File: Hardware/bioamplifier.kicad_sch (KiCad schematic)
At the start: 28 parts, among them J1 Conn_01x40_Pin, U1 ADS1299IPAG, U7 TPS73133DBV, U8 TPS73201DCQ, X1 ECS-2520MV-xxx-xx

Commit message: Add files via upload
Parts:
- removed C26: 1 nF, Capacitor_SMD:C_0603_1608Metric_Pad1.08x0.95mm_HandSolder, symbol Device:C_Small
- removed X1: ECS-2520MV-xxx-xx, Oscillator:Oscillator_SMD_ECS_2520MV-xxx-xx-4Pin_2.5x2.0mm, symbol Oscillator:ECS-2520MV-xxx-xx
- added C40: 1 nF, Capacitor_SMD:C_0201_0603Metric, symbol Device:C_Small
- added C41: 0.1 nF, Capacitor_SMD:C_0201_0603Metric, symbol Device:C_Small
- added JP2: Jumper_2_Bridged, Jumper:SolderJumper-2_P1.3mm_Bridged2Bar_Pad1.0x1.5mm, symbol Jumper:Jumper_2_Bridged
- C1, C10, C19, C2, C20, C21, C22, C23, C24, C25, C27, C3, C4, C5, C6, C7, C8, C9: footprint Capacitor_SMD:C_0603_1608Metric_Pad1.08x0.95mm_HandSolder -> Capacitor_SMD:C_0201_0603Metric
- C29: footprint (none) -> Capacitor_SMD:C_0201_0603Metric
- JP1: footprint (none) -> Jumper:SolderJumper-2_P1.3mm_Bridged2Bar_Pad1.0x1.5mm
- R21: footprint (none) -> Resistor_SMD:R_0201_0603Metric
- U1: footprint Ads1299:PAG64_TEX -> ads1299 8channel:PAG64_TEX
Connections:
- net 3.3V_UNREG: now also C27.1
- net 5V_UNREG: now also C40.1
- net BIASINV: now also JP2.1 (A)
- net DVDD: now also C41.1
- net GNDA: now also C27.2, C29.2, U7.2 (GND), C40.2, C41.2, JP2.2 (B)
- net GNDD: now also U1.37 (CLK); no longer C27.2, C29.2, U7.2 (GND)
- net GPIO1: now also J1.31 (Pin_31); no longer J1.16 (Pin_16)
- net GPIO2: now also J1.32 (Pin_32); no longer J1.18 (Pin_18)
- net GPIO3: now also J1.33 (Pin_33); no longer J1.20 (Pin_20)
- net GPIO4: now also J1.36 (Pin_36); no longer J1.22 (Pin_22)
- removed net CLK: C27.1, U1.37 (CLK)
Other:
- note added: "8 channels at 24 bit resolution ---> minimun clock rate 110khz"
- moved on the sheet: C29, U7

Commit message: redone analog inputs, passive component footprints now match real components, added library for possible 4 element capacitor array
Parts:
- removed JP1: Jumper_2_Bridged, Jumper:SolderJumper-2_P1.3mm_Bridged2Bar_Pad1.0x1.5mm, symbol Jumper:Jumper_2_Bridged
- removed R21: 1K, Resistor_SMD:R_0201_0603Metric, symbol Device:R_Small_US
- added R1: 1K, Resistor_SMD:R_0603_1608Metric, symbol Device:R_Small_US
- C1, C19, C2, C20, C21, C4, C6, C7: footprint Capacitor_SMD:C_0201_0603Metric -> Capacitor_SMD:C_0402_1005Metric
- C10, C22, C23, C24, C25, C27, C29, C3, C40, C41, C5, C8: footprint Capacitor_SMD:C_0201_0603Metric -> Capacitor_SMD:C_0603_1608Metric
- C9: footprint Capacitor_SMD:C_0201_0603Metric -> Capacitor_SMD:C_0805_2012Metric
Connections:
- net GNDD: no longer U1.64 (RESERVED)
- net GPIO1: now also R1.2; no longer U1.42 (GPIO1)
- net SCLK: now also U1.40 (SCLK)
- net SRB2: now also U1.18 (SRB2)
- net at D1.2 (A): now also U1.42 (GPIO1); no longer U1.40 (SCLK)
- net at D1.1 (K): now also R1.1

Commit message: redone analog inputs, decoupling caps
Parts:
- C22, C23, C24: footprint Capacitor_SMD:C_0603_1608Metric -> Capacitor_SMD:C_0402_1005Metric
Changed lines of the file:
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@@
 			)
 		)
-		(property "Footprint" "Capacitor_SMD:C_0603_1608Metric"
+		(property "Footprint" "Capacitor_SMD:C_0402_1005Metric"
 			(at 194.31 88.9 0)
 			(effects
@@
 			)
 		)
-		(property "Footprint" "Capacitor_SMD:C_0603_1608Metric"
+		(property "Footprint" "Capacitor_SMD:C_0402_1005Metric"
 			(at 231.14 76.2 0)
 			(effects
@@
 			)
 		)
-		(property "Footprint" "Capacitor_SMD:C_0603_1608Metric"
+		(property "Footprint" "Capacitor_SMD:C_0402_1005Metric"
 			(at 205.486 80.01 0)
 			(effects

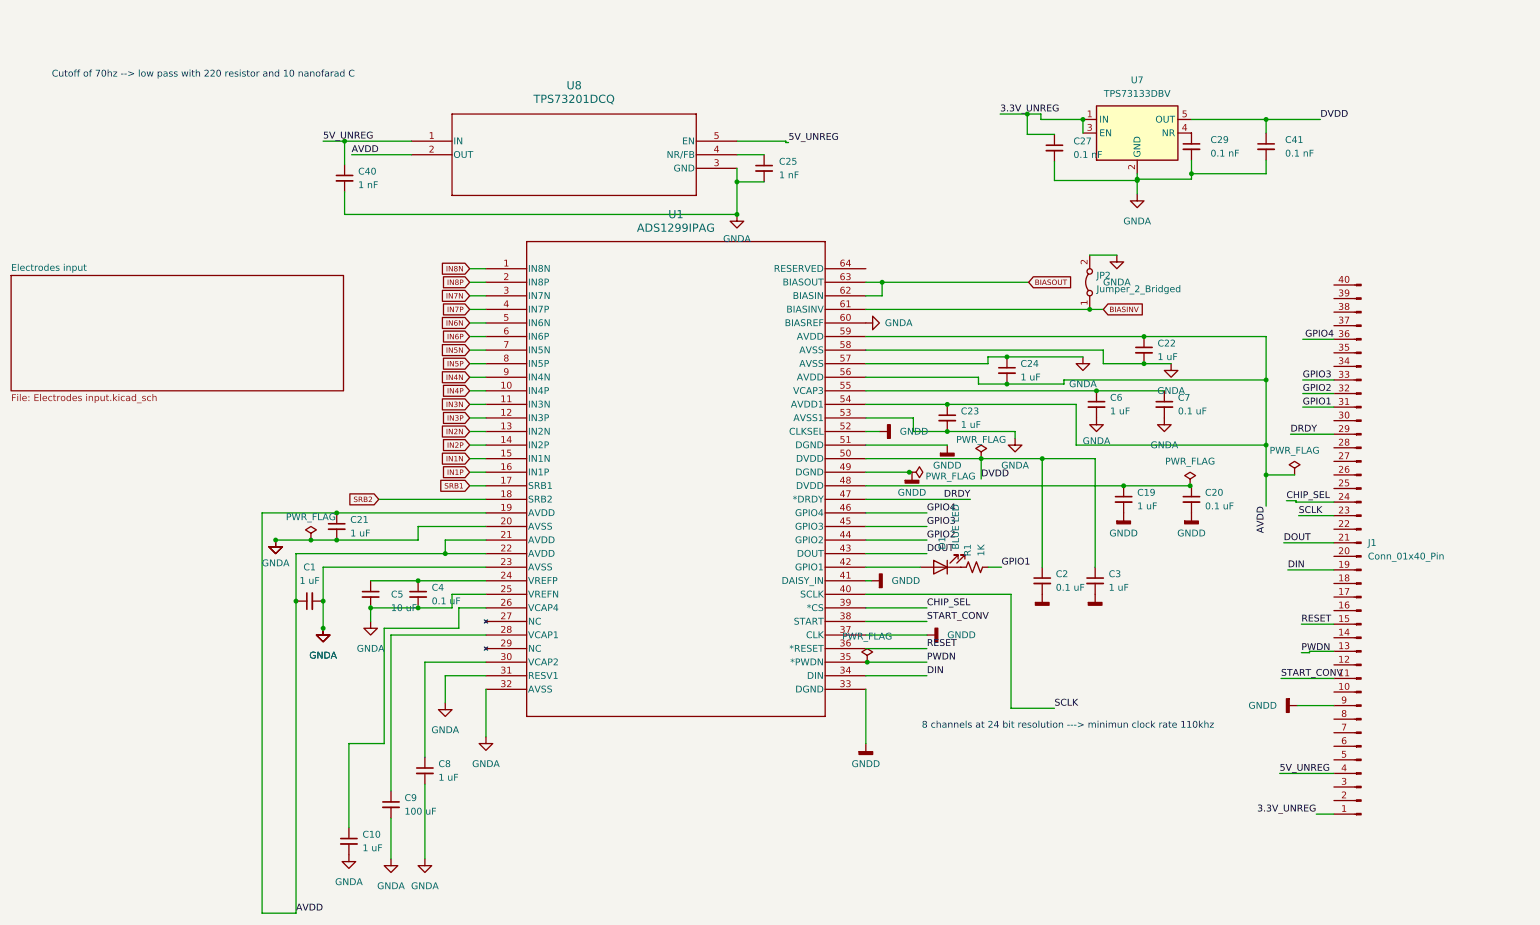
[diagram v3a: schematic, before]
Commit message: added schematics components for a bipolar power supply
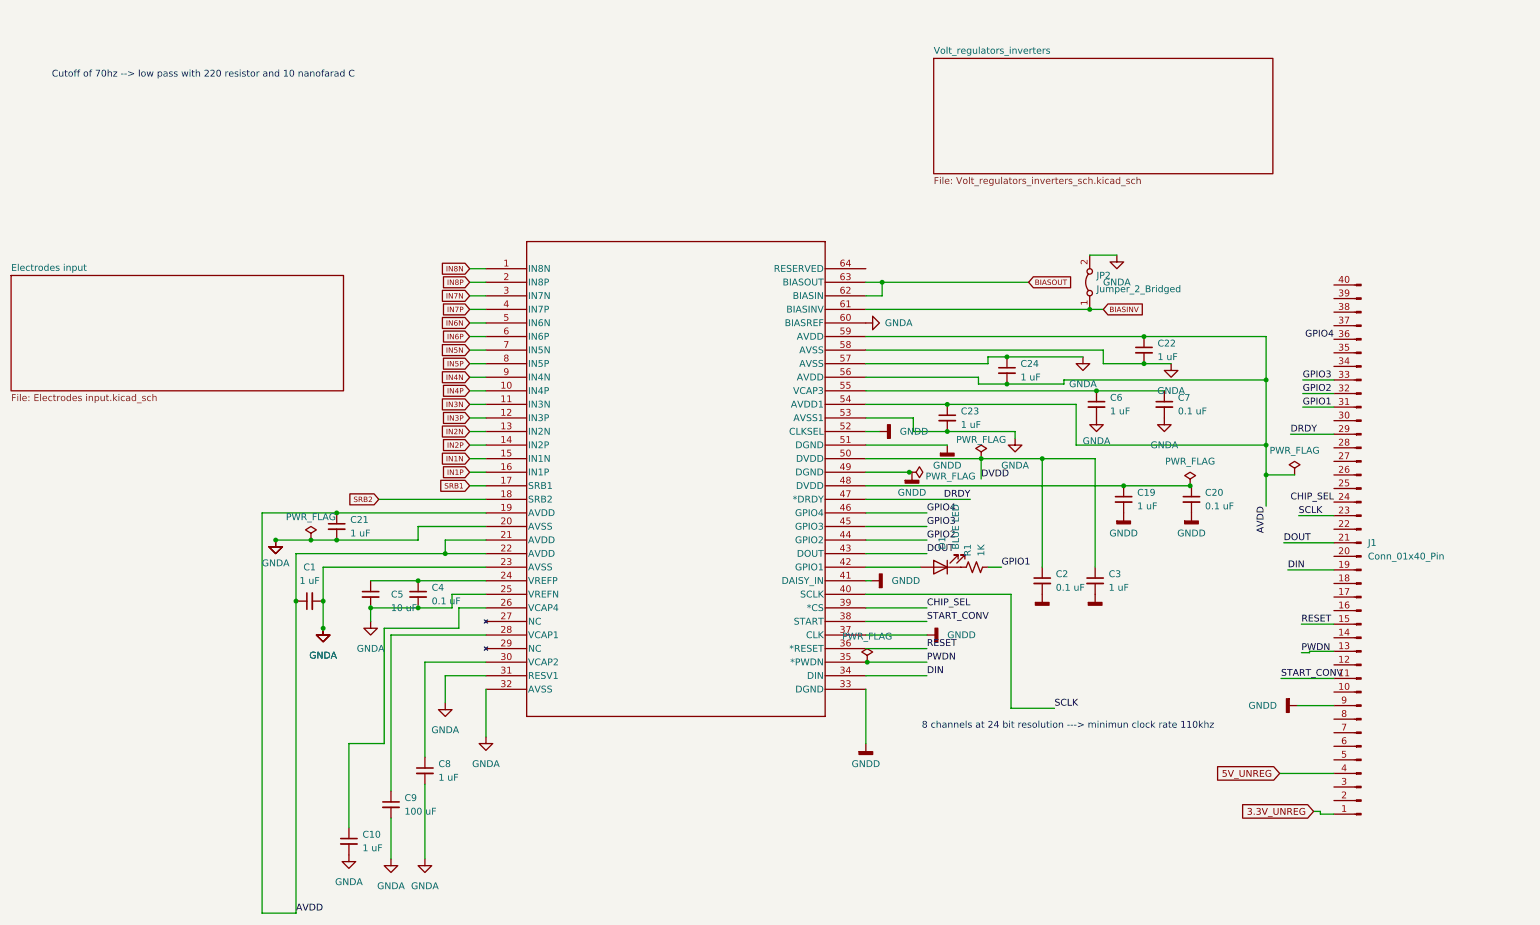
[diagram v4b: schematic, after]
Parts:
- removed C25, C40: 1 nF, Capacitor_SMD:C_0603_1608Metric, symbol Device:C_Small
- removed C27, C29, C41: 0.1 nF, Capacitor_SMD:C_0603_1608Metric, symbol Device:C_Small
- removed U7: TPS73133DBV, Package_TO_SOT_SMD:SOT-23-5, symbol Regulator_Linear:TPS73133DBV
- removed U8: TPS73201DCQ, tps732:DCQ6_TEX, symbol tps732:TPS73201DCQ
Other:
- added sheet Volt_regulators_inverters (Volt_regulators_inverters_sch.kicad_sch)

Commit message: first commit
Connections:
- net GNDA: now also C8.1; no longer C8.2
- net at U1.30 (VCAP2): now also C8.2; no longer C8.1
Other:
- moved on the sheet: C10, C21

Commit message: schematics redone, TODO: Pcb component placement
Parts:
- removed J1: Conn_01x40_Pin, Connector_PinHeader_2.54mm:PinHeader_2x20_P2.54mm_Vertical, symbol Connector:Conn_01x40_Pin
- added J1, J3: Conn_01x08_Socket, Connector_PinHeader_2.54mm:PinHeader_1x08_P2.54mm_Vertical, symbol Connector:Conn_01x08_Socket
- added R10, R11, R12, R13, R14, R15, R3, R4, R5, R6, R7, R8, R9: 50, Resistor_SMD:R_0402_1005Metric, symbol Device:R_Small_US
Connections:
- net 3.3V_UNREG: now also J3.7 (Pin_7)
- net 5V_UNREG: now also J3.8 (Pin_8)
- net CHIP_SEL: now also R6.1
- net DIN: now also R7.1
- net DOUT: now also R8.1
- net DRDY: now also R5.1
- net GNDA: now also C8.2; no longer C8.1
- net GNDD: now also J1.1 (Pin_1)
- net GPIO1: now also R12.1
- net GPIO2: now also R11.1
- net GPIO3: now also R10.1
- net GPIO4: now also R9.1
- net PWDN: now also R14.1
- net RESET: now also R13.1
- net SCLK: now also R3.1
- net START_CONV: now also R15.1, R4.1
- net at U1.30 (VCAP2): now also C8.1; no longer C8.2
- new net: J3.1 (Pin_1), R3.2
- new net: J3.5 (Pin_5), R7.2
- new net: J1.3 (Pin_3), R10.2
- new net: J1.4 (Pin_4), R11.2
- new net: J1.5 (Pin_5), R12.2
- new net: J1.2 (Pin_2), R9.2
- new net: J1.6 (Pin_6), R13.2
- new net: J1.8 (Pin_8), R15.2
- new net: J3.2 (Pin_2), R4.2
- new net: J1.7 (Pin_7), R14.2
- new net: J3.6 (Pin_6), R8.2
- new net: J3.4 (Pin_4), R6.2
- new net: J3.3 (Pin_3), R5.2
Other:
- moved on the sheet: C10, C19, C2, C24, C3, C4, C5, C7, C8, C9, JP2

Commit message: changes to pcb and schematics
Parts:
- removed J1: Conn_01x08_Socket, Connector_PinHeader_2.54mm:PinHeader_1x08_P2.54mm_Vertical, symbol Connector:Conn_01x08_Socket
- removed R15: 50, Resistor_SMD:R_0402_1005Metric, symbol Device:R_Small_US
- added J1: Conn_01x07_Socket, Connector_PinHeader_2.54mm:PinHeader_1x07_P2.54mm_Vertical, symbol Connector:Conn_01x07_Socket
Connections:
- net 3.3V_UNREG: now also J3.8 (Pin_8); no longer J3.7 (Pin_7)
- net 5V_UNREG: now also J3.7 (Pin_7); no longer J3.8 (Pin_8)
- net CHIP_SEL: now also R10.1; no longer R6.1
- net DIN: now also R14.1; no longer R7.1
- net DOUT: now also R7.1; no longer R8.1
- net DRDY: now also R3.1; no longer R5.1
- net GNDD: now also J1.1 (Pin_1)
- net GPIO1: now also R8.1; no longer R12.1
- net GPIO2: now also R6.1; no longer R11.1
- net GPIO3: now also R5.1; no longer R10.1
- net GPIO4: now also R4.1; no longer R9.1
- net PWDN: now also R13.1; no longer R14.1
- net RESET: now also R12.1; no longer R13.1
- net SCLK: now also R9.1; no longer R3.1
- net START_CONV: now also R11.1; no longer R4.1
- net at R10.2: now also J1.3 (Pin_3)
- net at R11.2: now also J1.4 (Pin_4)
- net at R12.2: now also J1.5 (Pin_5)
- net at R9.2: now also J1.2 (Pin_2)
- net at R13.2: now also J1.6 (Pin_6)
- net at R14.2: now also J1.7 (Pin_7)

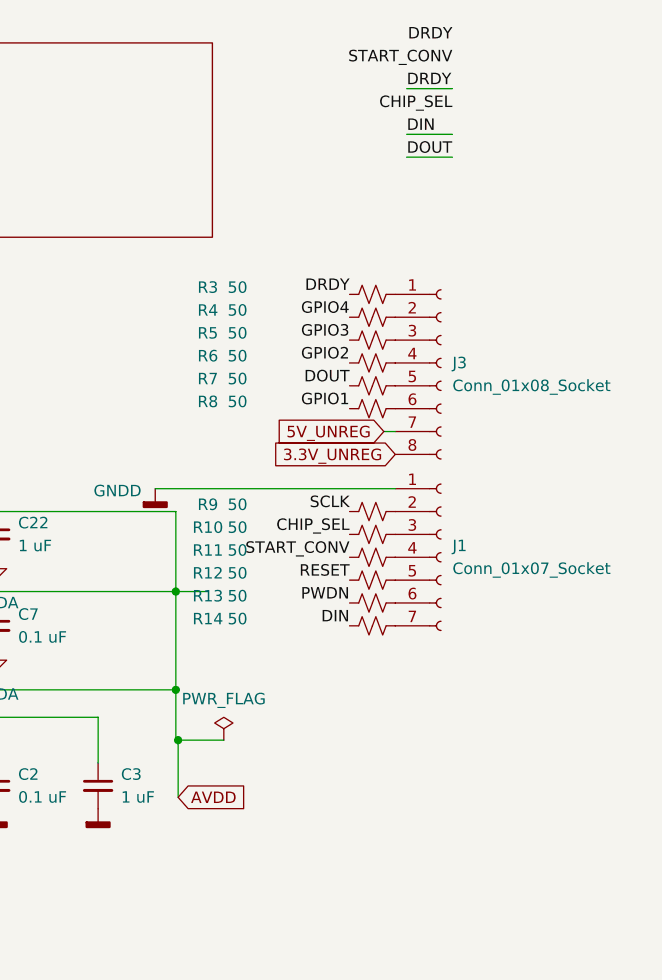
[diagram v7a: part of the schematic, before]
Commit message: removed 5V LDO Regulator
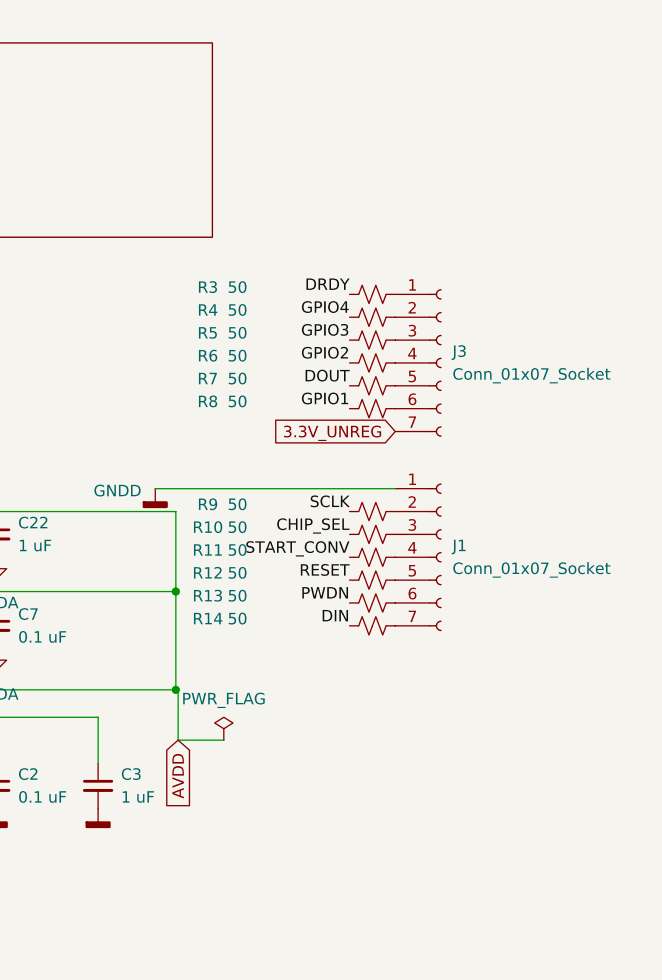
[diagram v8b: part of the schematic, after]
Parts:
- removed J3: Conn_01x08_Socket, Connector_PinHeader_2.54mm:PinHeader_1x08_P2.54mm_Vertical, symbol Connector:Conn_01x08_Socket
- added J3: Conn_01x07_Socket, Connector_PinHeader_2.54mm:PinHeader_1x07_P2.54mm_Vertical, symbol Connector:Conn_01x07_Socket
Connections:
- net 3.3V_UNREG: now also J3.7 (Pin_7)
- net at R3.2: now also J3.1 (Pin_1)
- net at R7.2: now also J3.5 (Pin_5)
- net at R4.2: now also J3.2 (Pin_2)
- net at R8.2: now also J3.6 (Pin_6)
- net at R6.2: now also J3.4 (Pin_4)
- net at R5.2: now also J3.3 (Pin_3)
